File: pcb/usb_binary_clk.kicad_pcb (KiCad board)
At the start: 2 copper layers, 55.6 x 77.4 mm, 43 parts, among them J1 USB_B_Micro, J2 USB_B_Micro, J3 AVR-ISP-6, SW1 SW_Push, SW2 SW_Push, SW3 SW_Push, U1 MCP7940N-xP, U2 ATtiny84V-10PU, Y1 Crystal

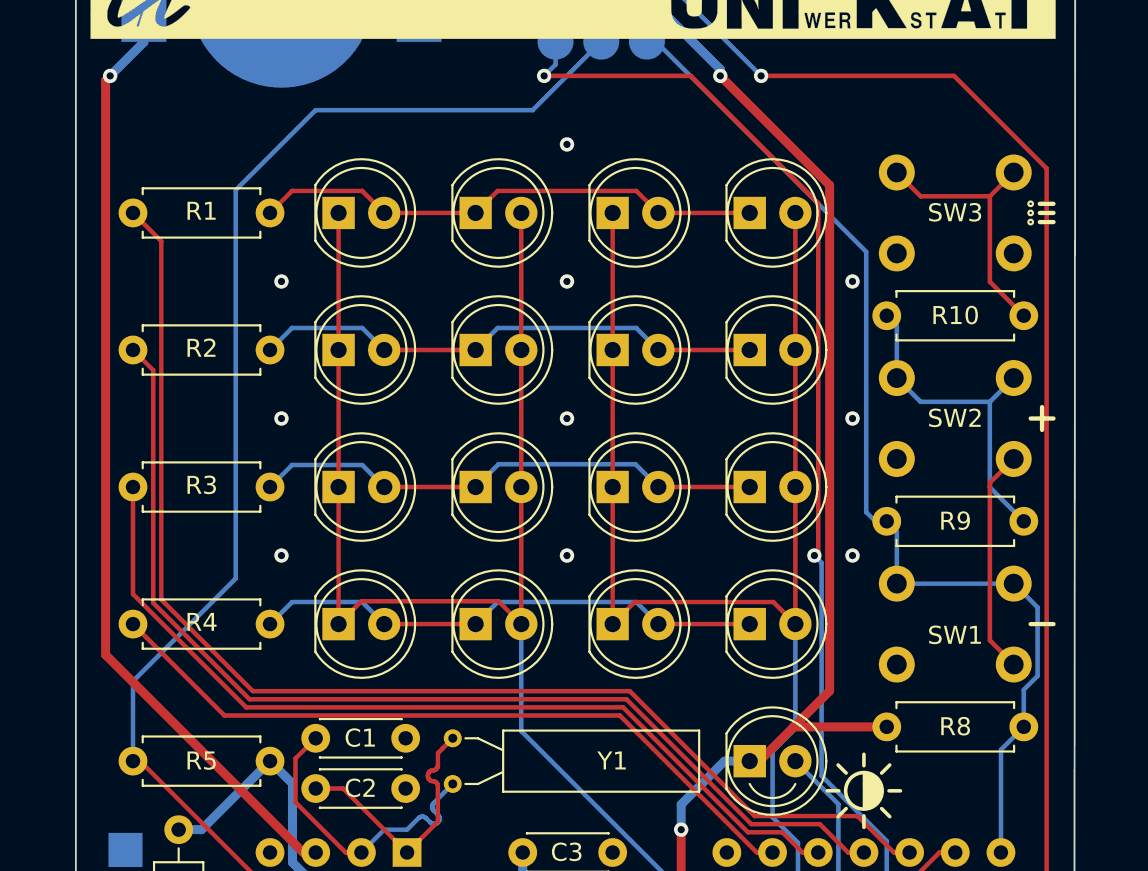
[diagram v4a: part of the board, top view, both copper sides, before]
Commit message: add mounting pads for stand/wall mount
fix #7
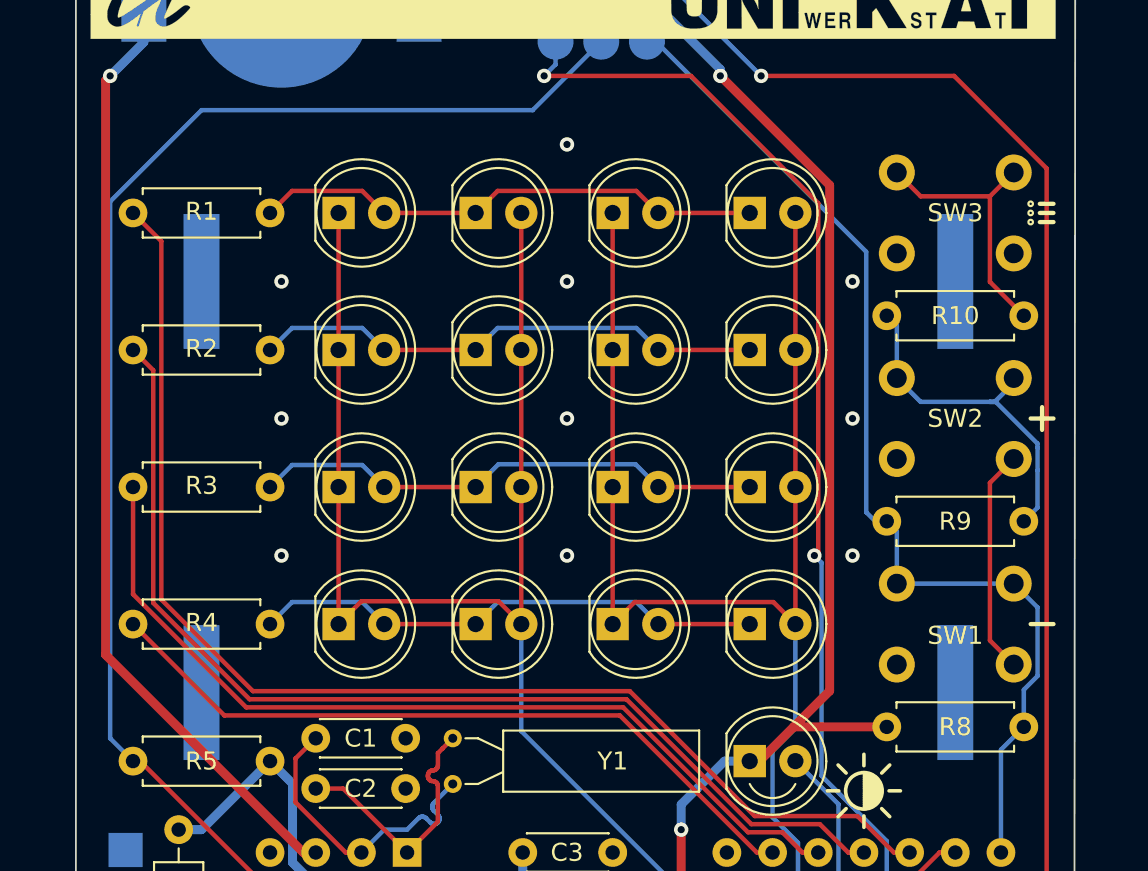
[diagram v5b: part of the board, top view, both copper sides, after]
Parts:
- added H1: MountingHole, binary_clk_parts:mountingPad_custom1, B.Cu at (133.3, 61.0)
- added H2: MountingHole, binary_clk_parts:mountingPad_custom1, B.Cu at (133.3, 83.8)
- added H3: MountingHole, binary_clk_parts:mountingPad_custom1, B.Cu at (175.3, 83.8)
- added H4: MountingHole, binary_clk_parts:mountingPad_custom1, B.Cu at (175.3, 61.0)
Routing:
- net /SCK: track 113.7 -> 118.5 mm
- net Net-(R10-Pad1): track 18.7 -> 19.7 mm
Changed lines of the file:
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@@
     (thickness 1.6)
     (drawings 332)
-    (tracks 310)
+    (tracks 317)
     (zones 0)
-    (modules 43)
+    (modules 47)
     (nets 31)
   )
@@
     (add_net "Net-(U2-Pad5)")
   )
+  (module binary_clk_parts:mountingPad_custom1 (layer B.Cu)
+    (at 133.35 60.96)
+    (fp_text reference H1 (at 0 -0.5) (layer B.SilkS)
+      (effects (font (size 1 1) (thickness 0.15)) (justify mirror))
+    )
+    (fp_text value MountingHole (at 0 0.5) (layer B.Fab)
+      (effects (font (size 1 1) (thickness 0.15)) (justify mirror))
+    )
+    (pad 1 smd rect (at 0 0) (size 2 7.5) (layers B.Cu B.Paste B.Mask))
+  )
+  (module binary_clk_parts:mountingPad_custom1 (layer B.Cu)
+    (at 175.26 60.96)
+    (fp_text reference H4 (at 0 -0.5) (layer B.SilkS)
+      (effects (font (size 1 1) (thickness 0.15)) (justify mirror))
+    )
+    (fp_text value MountingHole (at 0 0.5) (layer B.Fab)
+      (effects (font (size 1 1) (thickness 0.15)) (justify mirror))
+    )
+    (pad 1 smd rect (at 0 0) (size 2 7.5) (layers B.Cu B.Paste B.Mask))
+  )
+  (module binary_clk_parts:mountingPad_custom1 (layer B.Cu)
+    (at 175.26 83.82)
+    (fp_text reference H3 (at 0 -0.5) (layer B.SilkS)
+      (effects (font (size 1 1) (thickness 0.15)) (justify mirror))
+    )
+    (fp_text value MountingHole (at 0 0.5) (layer B.Fab)
+      (effects (font (size 1 1) (thickness 0.15)) (justify mirror))
+    )
+    (pad 1 smd rect (at 0 0) (size 2 7.5) (layers B.Cu B.Paste B.Mask))
+  )
+  (module binary_clk_parts:mountingPad_custom1 (layer B.Cu)
+    (at 133.35 83.82)
+    (fp_text reference H2 (at 0 -0.5) (layer B.SilkS)
+      (effects (font (size 1 1) (thickness 0.15)) (justify mirror))
+    )
+    (fp_text value MountingHole (at 0 0.5) (layer B.Fab)
+      (effects (font (size 1 1) (thickness 0.15)) (justify mirror))
+    )
+    (pad 1 smd rect (at 0 0) (size 2 7.5) (layers B.Cu B.Paste B.Mask))
+  )
   (module binary_clk_parts:qr_code_unikat (layer B.Cu)
     (at 171.45 46.355 180)
@@
   (segment (start 146.221642 90.328212) (end 146.192494 90.267686) (width 0.25) (layer B.Cu) (net 24))
   (segment (start 146.192494 90.267686) (end 146.177546 90.202192) (width 0.25) (layer B.Cu) (net 24))
-  (segment (start 177.184999 67.655001) (end 178.51 66.33) (width 0.25) (layer B.Cu) (net 25))
-  (segment (start 177.184999 72.409999) (end 177.184999 67.655001) (width 0.25) (layer B.Cu) (net 25))
-  (segment (start 179.07 74.295) (end 177.184999 72.409999) (width 0.25) (layer B.Cu) (net 25))
   (segment (start 172.01 63.425) (end 171.45 62.865) (width 0.25) (layer B.Cu) (net 25))
   (segment (start 172.01 66.33) (end 172.01 63.425) (width 0.25) (layer B.Cu) (net 25))
+  (segment (start 177.510001 67.655001) (end 177.184999 67.655001) (width 0.25) (layer B.Cu) (net 25))
+  (segment (start 179.835001 70.193999) (end 179.832 70.190998) (width 0.25) (layer B.Cu) (net 25))
+  (segment (start 179.832 69.977) (end 177.510001 67.655001) (width 0.25) (layer B.Cu) (net 25))
+  (segment (start 179.835001 71.466001) (end 179.835001 70.193999) (width 0.25) (layer B.Cu) (net 25))
+  (segment (start 179.832 71.469002) (end 179.835001 71.466001) (width 0.25) (layer B.Cu) (net 25))
+  (segment (start 179.832 70.190998) (end 179.832 69.977) (width 0.25) (layer B.Cu) (net 25))
+  (segment (start 179.832 73.533) (end 179.832 71.469002) (width 0.25) (layer B.Cu) (net 25))
+  (segment (start 179.07 74.295) (end 179.832 73.533) (width 0.25) (layer B.Cu) (net 25))
   (segment (start 173.335001 67.655001) (end 172.01 66.33) (width 0.25) (layer B.Cu) (net 25))
   (segment (start 177.184999 67.655001) (end 173.335001 67.655001) (width 0.25) (layer B.Cu) (net 25))
+  (segment (start 178.51 66.6) (end 178.51 66.33) (width 0.25) (layer B.Cu) (net 25))
+  (segment (start 177.454999 67.655001) (end 178.51 66.6) (width 0.25) (layer B.Cu) (net 25))
+  (segment (start 177.184999 67.655001) (end 177.454999 67.655001) (width 0.25) (layer B.Cu) (net 25))
   (segment (start 177.184999 56.225001) (end 178.51 54.9) (width 0.25) (layer F.Cu) (net 26))
   (segment (start 173.335001 56.225001) (end 172.01 54.9) (width 0.25) (layer F.Cu) (net 26))
@@
   (segment (start 175.26 92.71) (end 174.385002 92.71) (width 0.25) (layer F.Cu) (net 30))
   (segment (start 151.765 51.435) (end 155.575 47.625) (width 0.25) (layer B.Cu) (net 30))
-  (segment (start 139.7 51.435) (end 151.765 51.435) (width 0.25) (layer B.Cu) (net 30))
-  (segment (start 135.255 55.88) (end 139.7 51.435) (width 0.25) (layer B.Cu) (net 30))
-  (segment (start 135.255 77.47) (end 135.255 55.88) (width 0.25) (layer B.Cu) (net 30))
-  (segment (start 129.54 83.185) (end 135.255 77.47) (width 0.25) (layer B.Cu) (net 30))
-  (segment (start 129.54 87.63) (end 129.54 83.185) (width 0.25) (layer B.Cu) (net 30))
+  (segment (start 128.27 56.515) (end 133.35 51.435) (width 0.25) (layer B.Cu) (net 30))
+  (segment (start 128.27 86.36) (end 128.27 56.515) (width 0.25) (layer B.Cu) (net 30))
+  (segment (start 133.35 51.435) (end 151.765 51.435) (width 0.25) (layer B.Cu) (net 30))
+  (segment (start 129.54 87.63) (end 128.27 86.36) (width 0.25) (layer B.Cu) (net 30))
   (zone (net 1) (net_name GND) (layer B.Cu) (hatch edge 0.508)
     (connect_pads (clearance 0.508))

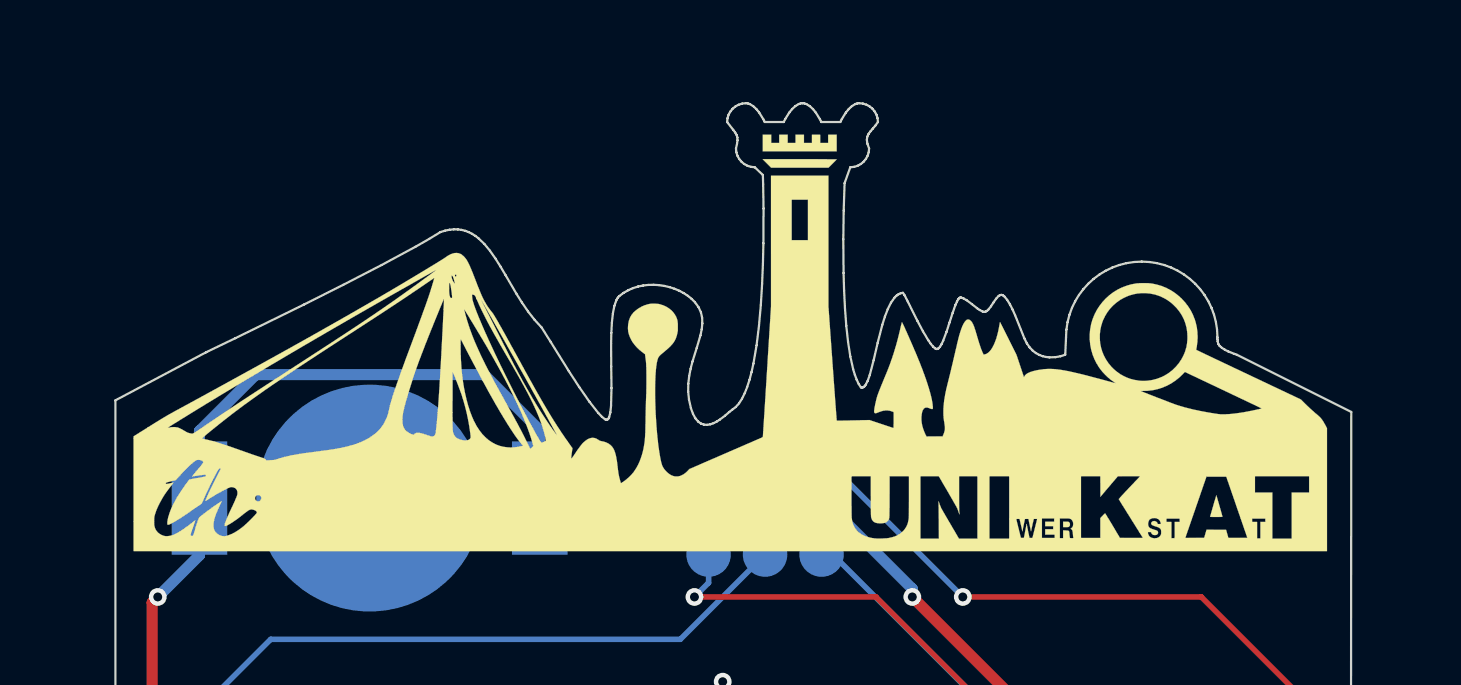
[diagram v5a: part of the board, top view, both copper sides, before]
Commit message: attempt to compensate for printing errors in silk screen
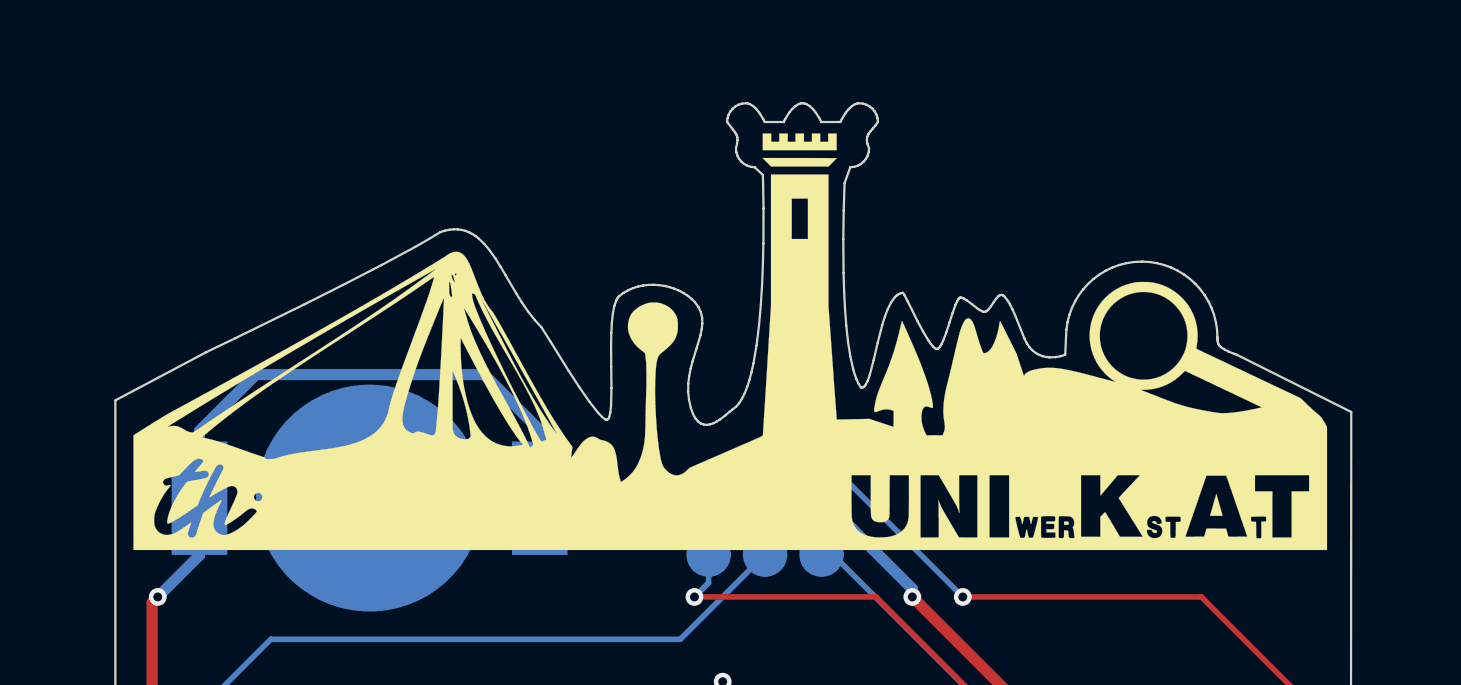
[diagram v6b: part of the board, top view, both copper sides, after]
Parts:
- moved G*** 0.05 mm to (154.1, 69.2)

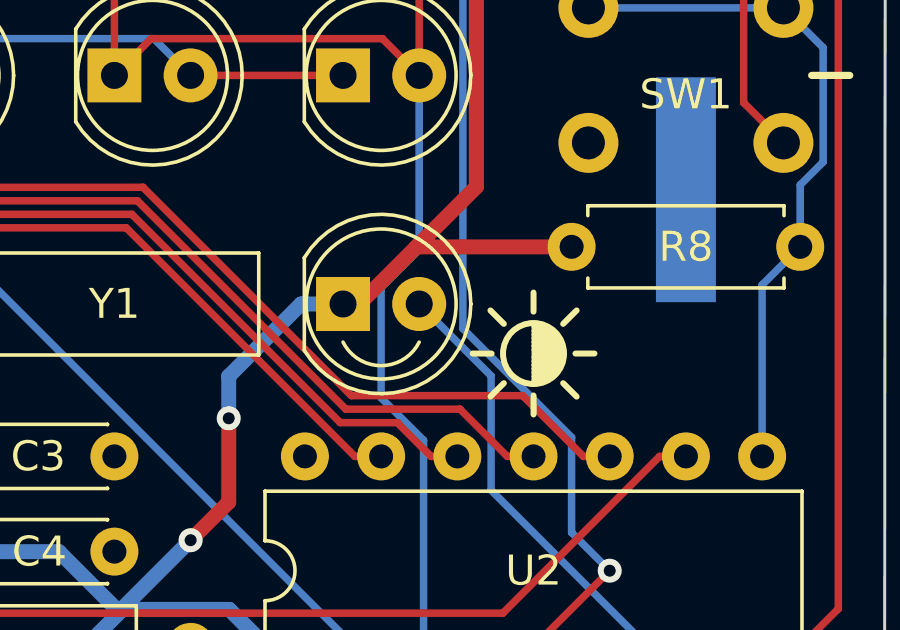
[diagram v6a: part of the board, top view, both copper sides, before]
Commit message: change photodiode footprint to 3mm
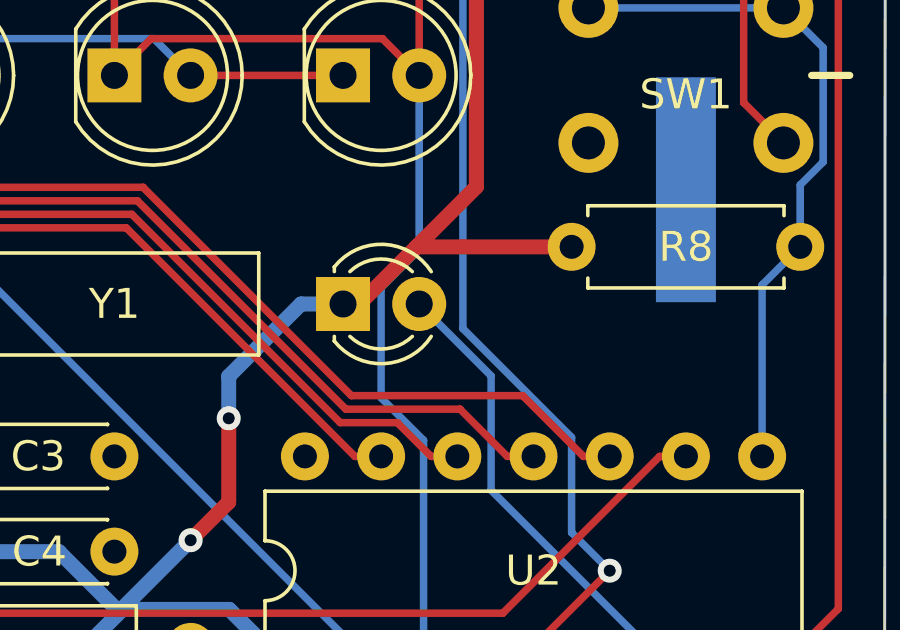
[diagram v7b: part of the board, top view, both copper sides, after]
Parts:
- D17: footprint custom:LED_D5.0mm -> LED_THT:LED_D3.0mm
- moved D17 1.27 mm to (163.8, 87.6)
